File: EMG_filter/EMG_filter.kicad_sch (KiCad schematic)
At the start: 13 parts, among them U1 AD620, U2 MCP6022

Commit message: new footprints for headers
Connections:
- net Output: now reaches Ce1.1, R7.1, U2.7
- net +3.3V renamed +In
- net -3V3 renamed -In
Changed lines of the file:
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@@
 		)
 	)
-	(symbol
-		(lib_id "power:-3V3")
-		(at 76.2 55.88 90)
-		(unit 1)
-		(exclude_from_sim no)
-		(in_bom yes)
-		(on_board yes)
-		(dnp no)
+	(global_label "-In"
+		(shape input)
+		(at 76.2 55.88 180)
 		(fields_autoplaced yes)
-		(property "Reference" "#PWR08"
-			(at 80.01 55.88 0)
+		(effects
+			(font
+				(size 1.27 1.27)
+			)
+			(justify right)
+		)
+		(property "Intersheetrefs" "${INTERSHEET_REFS}"
+			(at 69.8886 55.88 0)
 			(effects
 				(font
 					(size 1.27 1.27)
 				)
+				(justify right)
 				(hide yes)
 			)
 		)
-		(property "Value" "-3V3"
-			(at 72.39 55.8799 90)
+	)
+	(global_label "Output"
+		(shape output)
+		(at 232.41 80.01 0)
+		(fields_autoplaced yes)
+		(effects
+			(font
+				(size 1.27 1.27)
+			)
+			(justify left)
+		)
+		(property "Intersheetrefs" "${INTERSHEET_REFS}"
+			(at 241.6241 80.01 0)
 			(effects
 				(font
@@
 				)
 				(justify left)
+				(hide yes)
 			)
 		)
-		(property "Footprint" ""
-			(at 76.2 55.88 0)
+	)
+	(global_label "+In"
+		(shape input)
+		(at 76.2 90.17 180)
+		(fields_autoplaced yes)
+		(effects
+			(font
+				(size 1.27 1.27)
+			)
+			(justify right)
+		)
+		(property "Intersheetrefs" "${INTERSHEET_REFS}"
+			(at 69.8886 90.17 0)
 			(effects
 				(font
 					(size 1.27 1.27)
 				)
+				(justify right)
 				(hide yes)
-			)
-		)
-		(property "Datasheet" ""
-			(at 76.2 55.88 0)
-			(effects
-				(font
-					(size 1.27 1.27)
-				)
-				(hide yes)
-			)
-		)
-		(property "Description" "Power symbol creates a global label with name \"-3V3\""
-			(at 76.2 55.88 0)
-			(effects
-				(font
-					(size 1.27 1.27)
-				)
-				(hide yes)
-			)
-		)
-		(pin "1"
-		)
-		(instances
-			(project ""
-				(path "/08429b0a-9368-439a-9281-1b6be5b63174"
-					(reference "#PWR08")
-					(unit 1)
-				)
 			)
 		)
@@
 					(unit 1)
 				)
-			)
-		)
-	)
-	(symbol
-		(lib_id "power:+3.3V")
-		(at 76.2 90.17 90)
-		(unit 1)
-		(exclude_from_sim no)
-		(in_bom yes)
-		(on_board yes)
-		(dnp no)
-		(fields_autoplaced yes)
-		(property "Reference" "#PWR09"
-			(at 80.01 90.17 0)
-			(effects
-				(font
-					(size 1.27 1.27)
-				)
-				(hide yes)
-			)
-		)
-		(property "Value" "+3.3V"
-			(at 72.39 90.1699 90)
-			(effects
-				(font
-					(size 1.27 1.27)
-				)
-				(justify left)
-			)
-		)
-		(property "Footprint" ""
-			(at 76.2 90.17 0)
-			(effects
-				(font
-					(size 1.27 1.27)
-				)
-				(hide yes)
-			)
-		)
-		(property "Datasheet" ""
-			(at 76.2 90.17 0)
-			(effects
-				(font
-					(size 1.27 1.27)
-				)
-				(hide yes)
-			)
-		)
-		(property "Description" "Power symbol creates a global label with name \"+3.3V\""
-			(at 76.2 90.17 0)
-			(effects
-				(font
-					(size 1.27 1.27)
-				)
-				(hide yes)
-			)
-		)
-		(pin "1"
-		)
-		(instances
-			(project ""
-				(path "/08429b0a-9368-439a-9281-1b6be5b63174"
-					(reference "#PWR09")
-					(unit 1)
-				)

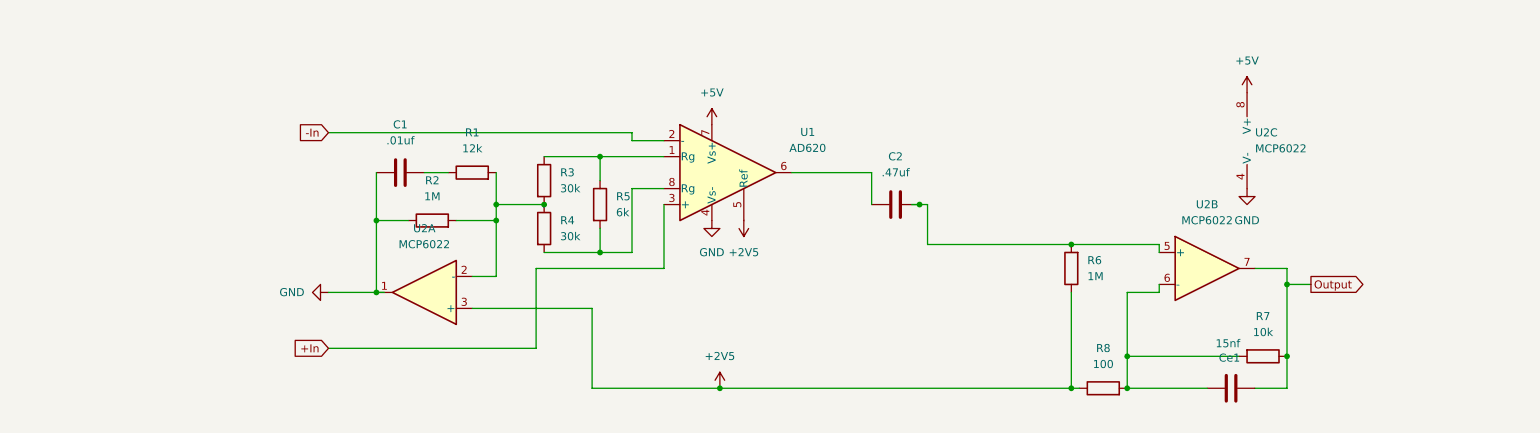
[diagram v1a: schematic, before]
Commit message: Remodeled PCB to have i/o
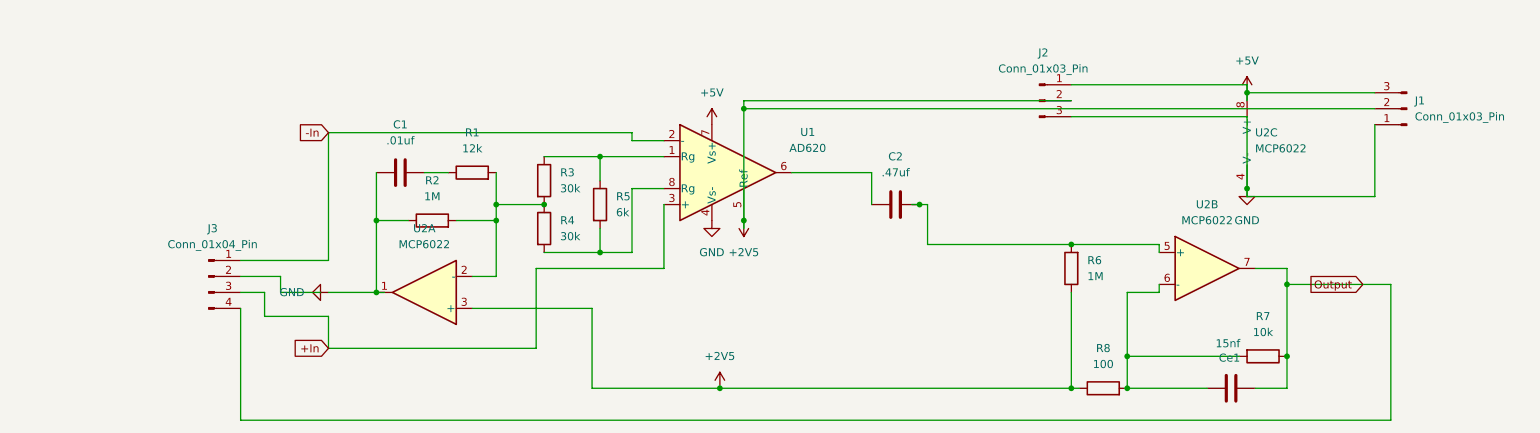
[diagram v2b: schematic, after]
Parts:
- added J1, J2: Conn_01x03_Pin, shared_footprints:CONN_SM03B-SRSS-TB_JST, symbol Connector:Conn_01x03_Pin
- added J3: Conn_01x04_Pin, shared_footprints:CONN_SM04B-SRSS-TB_JST, symbol Connector:Conn_01x04_Pin
- C1, C2, Ce1: footprint Capacitor_SMD:C_1206_3216Metric_Pad1.33x1.80mm_HandSolder -> Capacitor_SMD:C_0805_2012Metric_Pad1.18x1.45mm_HandSolder
- R1, R2, R3, R4, R5, R6, R7, R8: footprint Resistor_SMD:R_1206_3216Metric_Pad1.30x1.75mm_HandSolder -> Resistor_SMD:R_0805_2012Metric_Pad1.20x1.40mm_HandSolder
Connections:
- net +2V5: now also J1.2 (Pin_2), J2.2 (Pin_2)
- net +5V: now also J1.3 (Pin_3), J2.1 (Pin_1)
- net +In: now also J3.3 (Pin_3)
- net -In: now also J3.1 (Pin_1)
- net GND: now also J1.1 (Pin_1), J2.3 (Pin_3)
- net Output: now also J3.4 (Pin_4)

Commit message: new filter
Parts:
- U1, U2: footprint Package_SO:SOIC-8-1EP_3.9x4.9mm_P1.27mm_EP2.29x3mm -> Package_DIP:DIP-8_W7.62mm
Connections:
- net +5V: now also J1.1 (Pin_1); no longer J1.3 (Pin_3)
- net GND: now also J1.3 (Pin_3); no longer C1.1, J1.1 (Pin_1), R2.1, U2.1
- net PATIENT_GND: now reaches J3.2 (Pin_2)
- net PATIENT_GND: now also C1.1, R2.1, U2.1
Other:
- moved on the sheet: J3

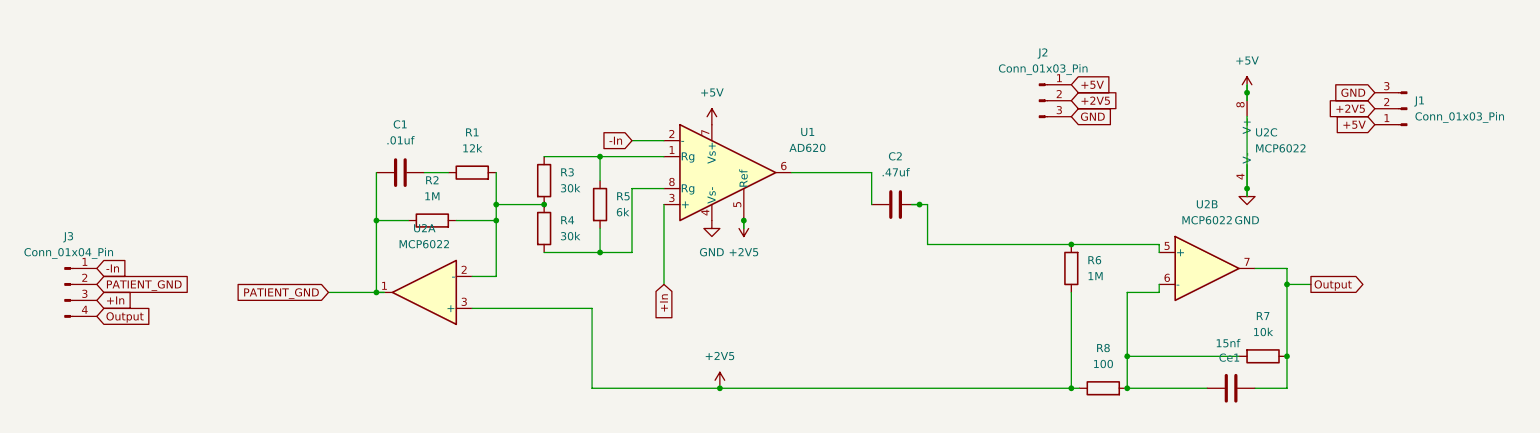
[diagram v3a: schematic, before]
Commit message: added decoupling caps, bit of rerouting
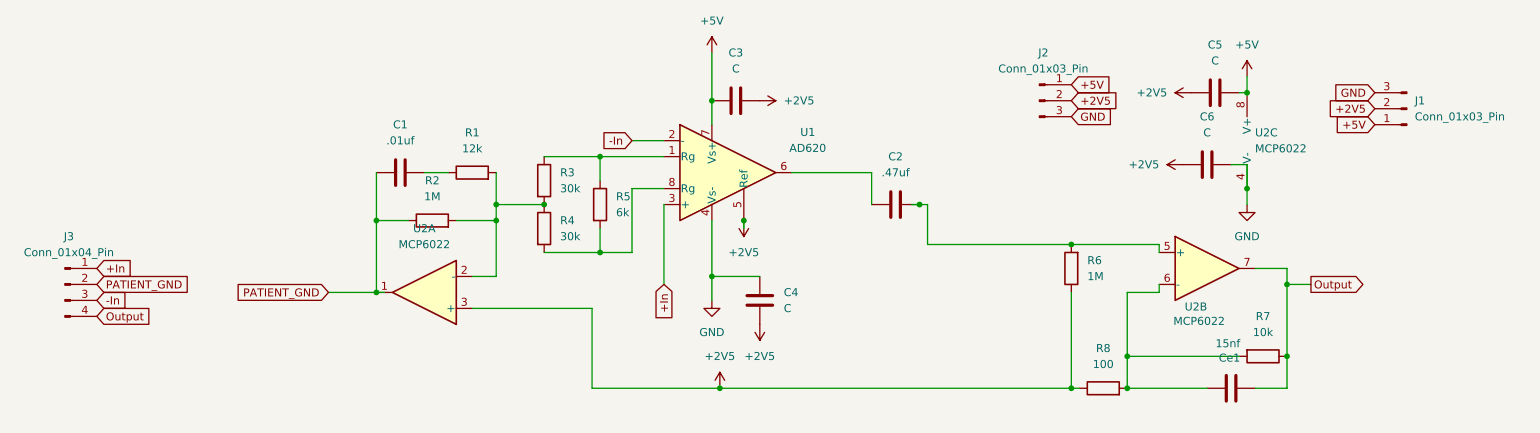
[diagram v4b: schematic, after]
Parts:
- added C3, C4, C5, C6: C, Capacitor_SMD:C_0805_2012Metric_Pad1.18x1.45mm_HandSolder, symbol Device:C
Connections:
- net +2V5: now also C3.2, C4.1, C5.1, C6.1
- net +5V: now also C3.1, C5.2
- net +In: now also J3.1 (Pin_1); no longer J3.3 (Pin_3)
- net -In: now also J3.3 (Pin_3); no longer J3.1 (Pin_1)
- net GND: now also C4.2, C6.2
